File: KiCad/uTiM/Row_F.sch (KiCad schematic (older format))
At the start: 10 parts, among them U601 APA102, U602 APA102, U603 APA102, U604 APA102, U605 APA102, U606 APA102, U607 APA102, U608 APA102

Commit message: microTiM aka uTiM work in progress
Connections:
- net CO_F renamed CI_G
- net DO_F renamed DI_G
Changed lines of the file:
@@
 DI_F
 Text HLabel 950  3100 0    60   Output ~ 12
-CO_F
+CI_G
 Text HLabel 950  2350 0    60   Input ~ 12
 GND
@@
 5V
 Text Label 1075 3100 0    60   ~ 0
-CO_F
+CI_G
 $Comp
 L GND #PWR06
@@
 	10950 3350 950  3350
 Text HLabel 950  3350 0    60   Output ~ 12
-DO_F
+DI_G
 Text HLabel 950  1400 0    60   Input ~ 12
 DI_F
@@
 	1300 1600 950  1600
 Text Label 1075 3350 0    60   ~ 0
-DO_F
+DI_G
 Text Label 1075 1600 0    60   ~ 0
 CI_F

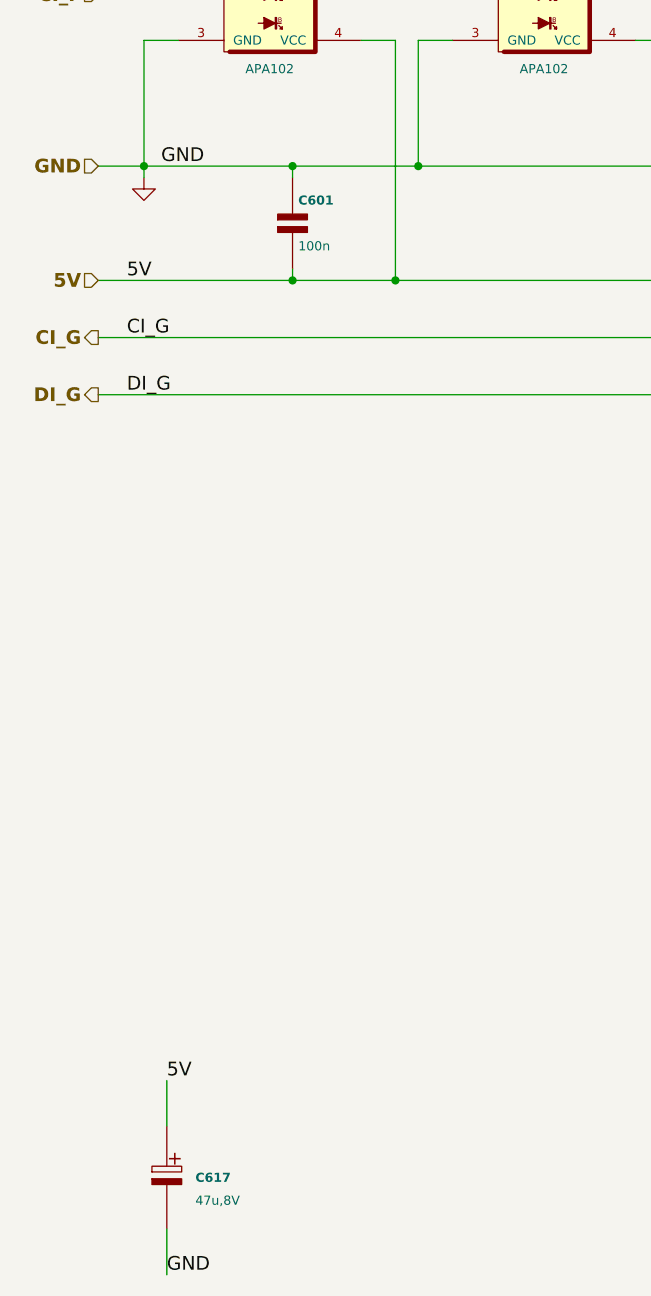
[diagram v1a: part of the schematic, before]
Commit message: work in progress, microTIM using APA102
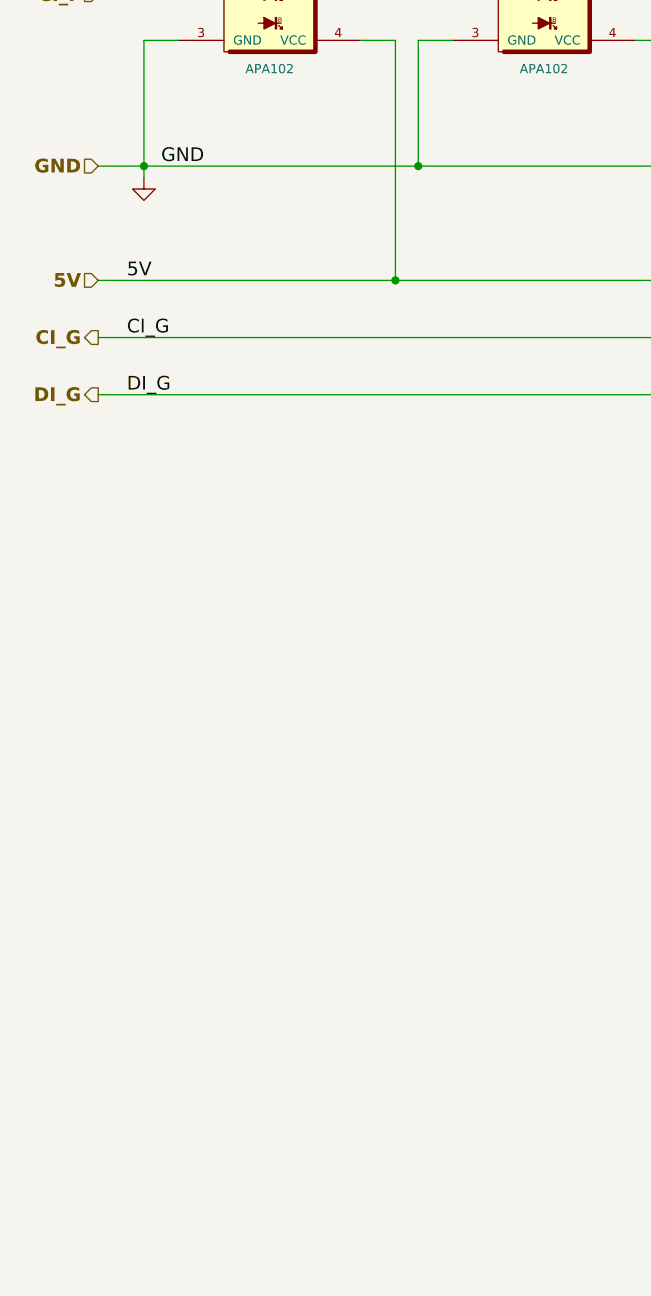
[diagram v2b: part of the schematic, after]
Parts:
- removed C601: 100n, TinyTiM_Libs:c_0805, symbol C2
- removed C617: 47u,8V, TinyTiM_Libs:c_2917, symbol C_POL_1
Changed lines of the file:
@@
 Comment4 ""
 $EndDescr
-$Comp
-L C2 C601
-U 1 1 5118AB55
-P 1800 2600
-F 0 "C601" H 1825 2700 40  0000 L CNB
-F 1 "100n" H 1825 2500 40  0000 L CNN
-F 2 "TinyTiM_Libs:c_0805" H 1800 2600 50  0001 C CNN
-F 3 "" H 1800 2600 60  0001 C CNN
-F 4 "CAP CER 0.1UF 25V 10% X7R 0805" H 1800 2800 60  0001 L CNN "Field4"
-F 5 "100nF, 25V" H 1800 2900 60  0001 L CNN "Field5"
-F 6 "Surface Mount, MLCC" H 1800 3000 60  0001 L CNN "Field6"
-F 7 "Kemet" H 1800 3100 60  0001 L CNN "Field7"
-F 8 "C0805C104K3RACTU" H 1800 3200 60  0001 L CNN "Field8"
-F 9 "Digikey" H 1800 3300 60  0001 L CNN "Field9"
-F 10 "399-1168-1-ND" H 1800 3400 60  0001 L CNN "Field10"
-F 11 "http://www.digikey.com/product-detail/en/C0805C104K3RACTU/399-1168-1-ND/411443" H 1800 3500 60  0001 L CNN "Field11"
-	1    1800 2600
-	1    0    0    -1
-$EndComp
-Text Label 1250 6350 0    60   ~ 0
-5V
-Text Label 1250 7200 0    60   ~ 0
-GND
-$Comp
-L C_POL_1 C617
-U 1 1 5118AB5F
-P 1250 6750
-F 0 "C617" H 1375 6725 40  0000 L CNB
-F 1 "47u,8V" H 1375 6625 40  0000 L CNN
-F 2 "TinyTiM_Libs:c_2917" H 1250 6700 50  0001 C CNN
-F 3 "" H 1250 6750 60  0001 C CNN
-F 4 "CAP ALUM 47UF 8V 20% SMD" H 1250 6950 60  0001 L CNN "Field4"
-F 5 "47u,8V" H 1250 7050 60  0001 L CNN "Field5"
-F 6 "2917 (7343 Metric)" H 1250 7150 60  0001 L CNN "Field6"
-F 7 "Panasonic Electronic Components" H 1250 7250 60  0001 L CNN "Field7"
-F 8 "EEF-CD0K470R" H 1250 7350 60  0001 L CNN "Field8"
-F 9 "Digikey" H 1250 7450 60  0001 L CNN "Field9"
-F 10 "PCE3606CT-ND" H 1250 7550 60  0001 L CNN "Field10"
-F 11 "http://www.digikey.com/product-detail/en/EEF-CD0K470R/PCE3606CT-ND/614442" H 1250 7650 60  0001 L CNN "Field11"
-	1    1250 6750
-	1    0    0    -1
-$EndComp
-Wire Wire Line
-	1250 7000 1250 7200
-Wire Wire Line
-	1250 6550 1250 6350
 Text Label 1075 1400 0    60   ~ 0
 DI_F
@@
 Wire Wire Line
 	1150 1800 1150 2400
-Connection ~ 1800 2850
-Wire Wire Line
-	1800 2850 1800 2800
 Wire Wire Line
 	950  3100 10800 3100
-Connection ~ 1800 2350
 Wire Wire Line
 	950  2350 9550 2350
@@
 	10800 3100 10800 1600
 Wire Wire Line
-	1800 2350 1800 2400
-Wire Wire Line
 	950  2850 10650 2850

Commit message: layout complete. Gerbers pending
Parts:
- renumbered U601 to U41, U602 to U42, U603 to U43, U604 to U44, U605 to U45, U606 to U46, U607 to U47, U608 to U48
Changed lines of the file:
@@
 GND
 $Comp
-L APA102 U601
+L APA102 U41
 U 1 1 56C21E5C
 P 1700 1600
-F 0 "U601" H 1700 1900 40  0000 C CNB
+F 0 "U41" H 1700 1900 40  0000 C CNB
 F 1 "APA102" H 1700 1275 40  0000 C CNN
 F 2 "TinyTiM_Libs:APA102" H 1600 2000 60  0001 C CNN
@@
 5V
 $Comp
-L APA102 U602
+L APA102 U42
 U 1 1 56C21E87
 P 2900 1600
-F 0 "U602" H 2900 1900 40  0000 C CNB
+F 0 "U42" H 2900 1900 40  0000 C CNB
 F 1 "APA102" H 2900 1275 40  0000 C CNN
 F 2 "TinyTiM_Libs:APA102" H 2800 2000 60  0001 C CNN
@@
 $EndComp
 $Comp
-L APA102 U603
+L APA102 U43
 U 1 1 56C21E8F
 P 4100 1600
-F 0 "U603" H 4100 1900 40  0000 C CNB
+F 0 "U43" H 4100 1900 40  0000 C CNB
 F 1 "APA102" H 4100 1275 40  0000 C CNN
 F 2 "TinyTiM_Libs:APA102" H 4000 2000 60  0001 C CNN
@@
 $EndComp
 $Comp
-L APA102 U604
+L APA102 U44
 U 1 1 56C21E97
 P 5300 1600
-F 0 "U604" H 5300 1900 40  0000 C CNB
+F 0 "U44" H 5300 1900 40  0000 C CNB
 F 1 "APA102" H 5300 1275 40  0000 C CNN
 F 2 "TinyTiM_Libs:APA102" H 5200 2000 60  0001 C CNN
@@
 $EndComp
 $Comp
-L APA102 U605
+L APA102 U45
 U 1 1 56C21E9F
 P 6500 1600
-F 0 "U605" H 6500 1900 40  0000 C CNB
+F 0 "U45" H 6500 1900 40  0000 C CNB
 F 1 "APA102" H 6500 1275 40  0000 C CNN
 F 2 "TinyTiM_Libs:APA102" H 6400 2000 60  0001 C CNN
@@
 $EndComp
 $Comp
-L APA102 U606
+L APA102 U46
 U 1 1 56C21EA7
 P 7700 1600
-F 0 "U606" H 7700 1900 40  0000 C CNB
+F 0 "U46" H 7700 1900 40  0000 C CNB
 F 1 "APA102" H 7700 1275 40  0000 C CNN
 F 2 "TinyTiM_Libs:APA102" H 7600 2000 60  0001 C CNN
@@
 $EndComp
 $Comp
-L APA102 U607
+L APA102 U47
 U 1 1 56C21EAF
 P 8900 1600
-F 0 "U607" H 8900 1900 40  0000 C CNB
+F 0 "U47" H 8900 1900 40  0000 C CNB
 F 1 "APA102" H 8900 1275 40  0000 C CNN
 F 2 "TinyTiM_Libs:APA102" H 8800 2000 60  0001 C CNN
@@
 $EndComp
 $Comp
-L APA102 U608
+L APA102 U48
 U 1 1 56C21EB7
 P 10100 1600
-F 0 "U608" H 10100 1900 40  0000 C CNB
+F 0 "U48" H 10100 1900 40  0000 C CNB
 F 1 "APA102" H 10100 1275 40  0000 C CNN
 F 2 "TinyTiM_Libs:APA102" H 10000 2000 60  0001 C CNN
